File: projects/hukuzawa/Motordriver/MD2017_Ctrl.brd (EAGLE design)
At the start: 65 x 65 mm, 18 parts, among them IC1 PIC16F648, J1 3X2A, Q1 CERALOCK

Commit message: モータドライバ制御部 ボード図一時完成
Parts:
- moved U$2 42.9 mm to (45.5, 4.00), turned to 180 degrees
- moved D3 39.0 mm to (59.0, 19.0), turned to 270 degrees
- moved POWERPPORT 27.5 mm to (67.0, 18.0), turned to 90 degrees
- moved POWERNPORT 24.2 mm to (3.00, 18.0), turned to 90 degrees
- moved U$3 21.6 mm to (14.0, 13.0), turned to 270 degrees
- moved Q1 16.4 mm to (32.5, 54.5), turned to 0 degrees
- moved D4 12.2 mm to (30.0, 18.5), turned to 90 degrees
- moved C2 6.96 mm to (57.0, 45.5)
- moved C1 6.80 mm to (62.5, 45.5)
- moved C3 6.80 mm to (52.0, 45.5)
- moved J1 6.36 mm to (66.0, 58.0)
- moved NJM1 5.85 mm to (60.0, 51.0)
- moved IC1 5.52 mm to (35.0, 45.5)
- moved D2 5.32 mm to (49.5, 24.0)
- moved SIGNALPORT 5.15 mm to (35.0, 65.0)
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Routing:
- net GND: track 0.00 -> 159.0 mm, vias 0 -> 4
- net 5V: track 0.00 -> 94.9 mm
- net N$3: track 0.00 -> 67.1 mm
- net N$7: track 0.00 -> 49.6 mm
- net SIGNAL: track 0.00 -> 46.1 mm, vias 0 -> 2
- net N$6: track 0.00 -> 40.7 mm
- net N$5: track 0.00 -> 35.8 mm
- net N$2: track 0.00 -> 35.6 mm
- net N$4: track 0.00 -> 35.5 mm
- net BDIR: track 0.00 -> 32.3 mm, vias 0 -> 2
- net ADIR: track 0.00 -> 22.0 mm, vias 0 -> 2
- net BPWM: track 0.00 -> 19.5 mm
- net BD/B: track 0.00 -> 19.5 mm
- net APWM: track 0.00 -> 19.5 mm
- net 9VIN: track 0.00 -> 18.6 mm
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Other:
- board size 65 x 65 mm -> 70 x 70 mm

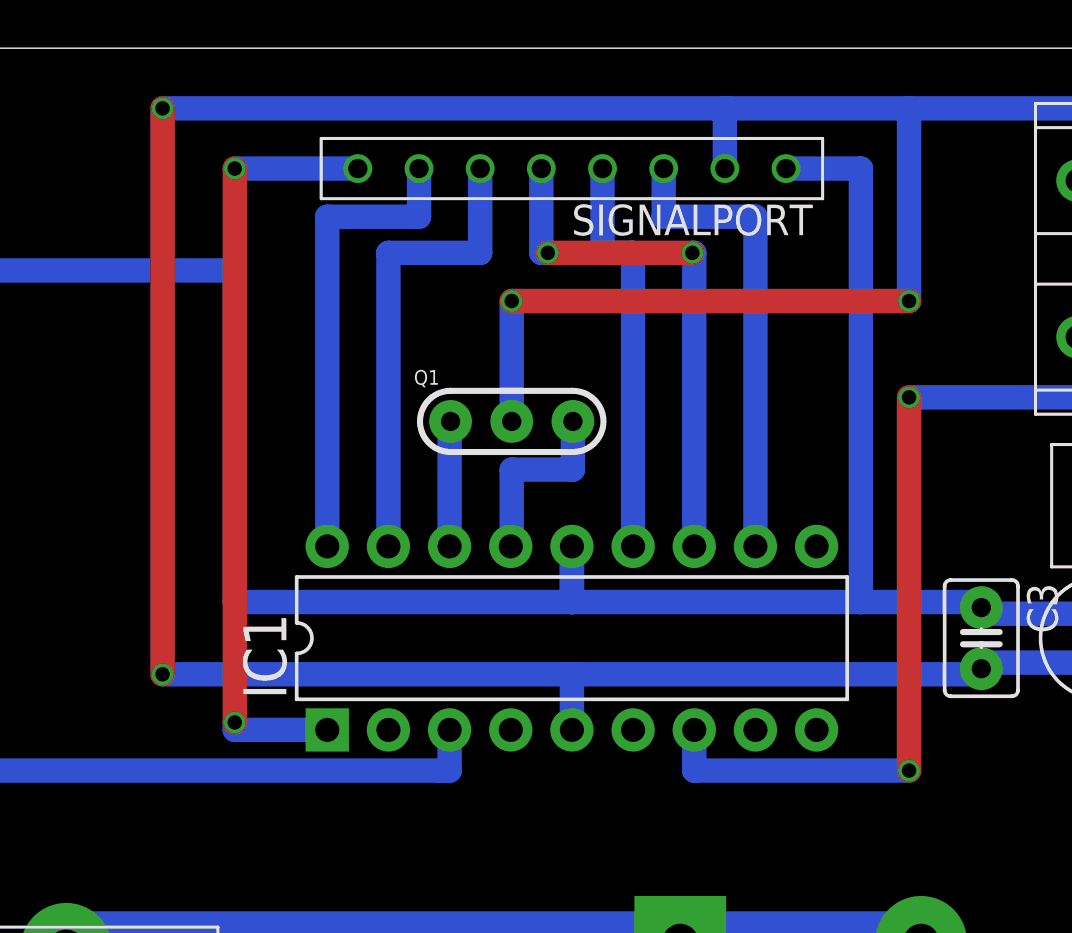
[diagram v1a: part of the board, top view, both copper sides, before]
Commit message: モータードライバ修正
モータードライバのジャンパ線部のドリル径を修正
それに伴って一部の配置の修正
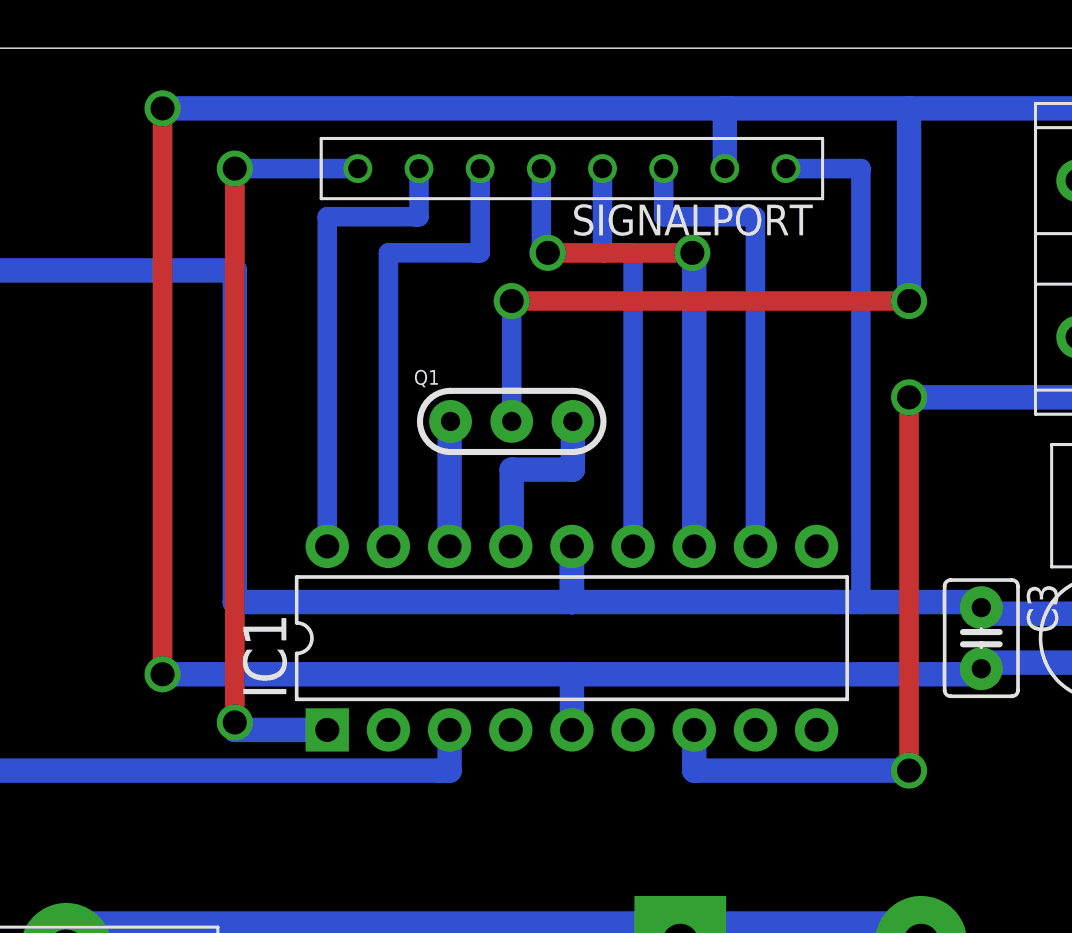
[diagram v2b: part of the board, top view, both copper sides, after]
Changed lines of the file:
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@@
 <wire x1="47" y1="47" x2="52" y2="47" width="1.016" layer="16"/>
 <wire x1="52" y1="47" x2="52" y2="46.77" width="1.016" layer="16"/>
-<wire x1="43.89" y1="65" x2="47" y2="65" width="1.016" layer="16"/>
-<wire x1="47" y1="65" x2="47" y2="47" width="1.016" layer="16"/>
+<wire x1="43.89" y1="65" x2="47" y2="65" width="0.8128" layer="16"/>
+<wire x1="47" y1="65" x2="47" y2="47" width="0.8128" layer="16"/>
 </signal>
 <signal name="9VIN">
@@
 <wire x1="40.08" y1="41.69" x2="40.08" y2="40" width="1.016" layer="16"/>
 <wire x1="40.08" y1="40" x2="49" y2="40" width="1.016" layer="16"/>
-<via x="49" y="40" extent="1-16" drill="0.6" shape="square"/>
-<wire x1="49" y1="40" x2="49" y2="55.5" width="1.016" layer="1"/>
-<via x="49" y="55.5" extent="1-16" drill="0.6" shape="square"/>
+<via x="49" y="40" extent="1-16" drill="1"/>
+<wire x1="49" y1="40" x2="49" y2="55.5" width="0.8128" layer="1"/>
+<via x="49" y="55.5" extent="1-16" drill="1"/>
 <wire x1="49" y1="55.5" x2="60" y2="55.5" width="1.016" layer="16"/>
 <wire x1="60" y1="55.5" x2="60" y2="58" width="1.016" layer="16"/>
@@
 <wire x1="35" y1="41.69" x2="35" y2="44" width="1.016" layer="16"/>
 <wire x1="35" y1="44" x2="18" y2="44" width="1.016" layer="16"/>
-<via x="18" y="44" extent="1-16" drill="0.6" shape="square"/>
-<wire x1="18" y1="44" x2="18" y2="67.5" width="1.016" layer="1"/>
-<via x="18" y="67.5" extent="1-16" drill="0.6" shape="square"/>
+<via x="18" y="44" extent="1-16" drill="1"/>
+<wire x1="18" y1="44" x2="18" y2="67.5" width="0.8128" layer="1"/>
+<via x="18" y="67.5" extent="1-16" drill="1"/>
 <wire x1="18" y1="67.5" x2="41.5" y2="67.5" width="1.016" layer="16"/>
 <wire x1="35" y1="44" x2="52" y2="44" width="1.016" layer="16"/>
 <wire x1="52" y1="44" x2="52" y2="44.23" width="1.016" layer="16"/>
-<wire x1="32.5" y1="54.5" x2="32.5" y2="59.5" width="1.016" layer="16"/>
-<via x="32.5" y="59.5" extent="1-16" drill="0.6" shape="square"/>
-<wire x1="32.5" y1="59.5" x2="49" y2="59.5" width="1.016" layer="1"/>
-<via x="49" y="59.5" extent="1-16" drill="0.6" shape="square"/>
+<wire x1="32.5" y1="54.5" x2="32.5" y2="59.5" width="0.8128" layer="16"/>
+<via x="32.5" y="59.5" extent="1-16" drill="1"/>
+<wire x1="32.5" y1="59.5" x2="49" y2="59.5" width="0.8128" layer="1"/>
+<via x="49" y="59.5" extent="1-16" drill="1"/>
 <wire x1="49" y1="59.5" x2="49" y2="67.5" width="1.016" layer="16"/>
 </signal>
@@
 <contactref element="SIGNALPORT" pad="3"/>
 <contactref element="IC1" pad="11"/>
-<wire x1="38.81" y1="65" x2="38.81" y2="63" width="1.016" layer="16"/>
-<wire x1="38.81" y1="63" x2="42.5" y2="63" width="1.016" layer="16"/>
-<wire x1="42.5" y1="63" x2="42.62" y2="63" width="1.016" layer="16"/>
-<wire x1="42.62" y1="63" x2="42.62" y2="49.31" width="1.016" layer="16"/>
+<wire x1="38.81" y1="65" x2="38.81" y2="63" width="0.8128" layer="16"/>
+<wire x1="38.81" y1="63" x2="42.5" y2="63" width="0.8128" layer="16"/>
+<wire x1="42.5" y1="63" x2="42.62" y2="63" width="0.8128" layer="16"/>
+<wire x1="42.62" y1="63" x2="42.62" y2="49.31" width="0.8128" layer="16"/>
 </signal>
 <signal name="AD/B">
 <contactref element="SIGNALPORT" pad="4"/>
 <contactref element="IC1" pad="13"/>
-<wire x1="36.27" y1="65" x2="36.27" y2="61.5" width="1.016" layer="16"/>
-<wire x1="36.27" y1="61.5" x2="37.5" y2="61.5" width="1.016" layer="16"/>
-<wire x1="37.5" y1="61.5" x2="37.54" y2="61.5" width="1.016" layer="16"/>
-<wire x1="37.54" y1="61.5" x2="37.54" y2="49.31" width="1.016" layer="16"/>
+<wire x1="36.27" y1="65" x2="36.27" y2="61.5" width="0.8128" layer="16"/>
+<wire x1="36.27" y1="61.5" x2="37.5" y2="61.5" width="0.8128" layer="16"/>
+<wire x1="37.5" y1="61.5" x2="37.54" y2="61.5" width="0.8128" layer="16"/>
+<wire x1="37.54" y1="61.5" x2="37.54" y2="49.31" width="0.8128" layer="16"/>
 </signal>
 <signal name="ADIR">
 <contactref element="SIGNALPORT" pad="5"/>
 <contactref element="IC1" pad="12"/>
-<wire x1="33.73" y1="65" x2="33.73" y2="61.5" width="1.016" layer="16"/>
+<wire x1="33.73" y1="65" x2="33.73" y2="61.5" width="0.8128" layer="16"/>
 <wire x1="33.73" y1="61.5" x2="34" y2="61.5" width="1.016" layer="16"/>
-<via x="34" y="61.5" extent="1-16" drill="0.6" shape="square"/>
-<wire x1="34" y1="61.5" x2="40" y2="61.5" width="1.016" layer="1"/>
-<via x="40" y="61.5" extent="1-16" drill="0.6" shape="square"/>
+<via x="34" y="61.5" extent="1-16" drill="1"/>
+<wire x1="34" y1="61.5" x2="40" y2="61.5" width="0.8128" layer="1"/>
+<via x="40" y="61.5" extent="1-16" drill="1"/>
 <wire x1="40" y1="61.5" x2="40.08" y2="61.5" width="1.016" layer="16"/>
 <wire x1="40.08" y1="61.5" x2="40.08" y2="49.31" width="1.016" layer="16"/>
@@
 <contactref element="SIGNALPORT" pad="6"/>
 <contactref element="IC1" pad="17"/>
-<wire x1="27.38" y1="49.31" x2="27.38" y2="61.5" width="1.016" layer="16"/>
-<wire x1="27.38" y1="61.5" x2="31" y2="61.5" width="1.016" layer="16"/>
-<wire x1="31" y1="61.5" x2="31.19" y2="61.5" width="1.016" layer="16"/>
-<wire x1="31.19" y1="61.5" x2="31.19" y2="65" width="1.016" layer="16"/>
+<wire x1="27.38" y1="49.31" x2="27.38" y2="61.5" width="0.8128" layer="16"/>
+<wire x1="27.38" y1="61.5" x2="31" y2="61.5" width="0.8128" layer="16"/>
+<wire x1="31" y1="61.5" x2="31.19" y2="61.5" width="0.8128" layer="16"/>
+<wire x1="31.19" y1="61.5" x2="31.19" y2="65" width="0.8128" layer="16"/>
 </signal>
 <signal name="BD/B">
 <contactref element="SIGNALPORT" pad="7"/>
 <contactref element="IC1" pad="18"/>
-<wire x1="24.84" y1="49.31" x2="24.84" y2="63" width="1.016" layer="16"/>
-<wire x1="24.84" y1="63" x2="28.5" y2="63" width="1.016" layer="16"/>
-<wire x1="28.5" y1="63" x2="28.65" y2="63" width="1.016" layer="16"/>
-<wire x1="28.65" y1="63" x2="28.65" y2="65" width="1.016" layer="16"/>
+<wire x1="24.84" y1="49.31" x2="24.84" y2="63" width="0.8128" layer="16"/>
+<wire x1="24.84" y1="63" x2="28.5" y2="63" width="0.8128" layer="16"/>
+<wire x1="28.5" y1="63" x2="28.65" y2="63" width="0.8128" layer="16"/>
+<wire x1="28.65" y1="63" x2="28.65" y2="65" width="0.8128" layer="16"/>
 </signal>
 <signal name="BDIR">
 <contactref element="SIGNALPORT" pad="8"/>
 <contactref element="IC1" pad="1"/>
-<wire x1="26.11" y1="65" x2="21" y2="65" width="1.016" layer="16"/>
-<via x="21" y="65" extent="1-16" drill="0.6" shape="square"/>
-<wire x1="21" y1="65" x2="21" y2="42" width="1.016" layer="1"/>
-<via x="21" y="42" extent="1-16" drill="0.6" shape="square"/>
+<wire x1="26.11" y1="65" x2="21" y2="65" width="0.8128" layer="16"/>
+<via x="21" y="65" extent="1-16" drill="1"/>
+<wire x1="21" y1="65" x2="21" y2="42" width="0.8128" layer="1"/>
+<via x="21" y="42" extent="1-16" drill="1"/>
 <wire x1="21" y1="42" x2="21" y2="41.69" width="1.016" layer="16"/>
 <wire x1="21" y1="41.69" x2="24.84" y2="41.69" width="1.016" layer="16"/>

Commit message: モータードライバ修正
穴径を1.0～1.2mmの範囲に収まるよう修正
Dimensionラインの太さを0に修正
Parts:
- D1, D2, D3, D4: device FP-21T for MITS:DO201-15 -> diode:DO201-15
- moved D1 14.4 mm to (25.5, 20.5)
- moved D4 13.5 mm to (41.5, 11.5), turned to 180 degrees
- moved D2 9.71 mm to (41.5, 29.5), turned to 180 degrees
- moved D3 1.80 mm to (58.0, 20.5)
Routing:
- net N$6: track 40.7 -> 15.3 mm
- net N$5: track 35.8 -> 22.2 mm
- net N$7: track 49.6 -> 37.0 mm
- net N$3: track 67.1 -> 55.7 mm
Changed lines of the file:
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@@
 <element name="POWERPPORT" library="FH105" package="FH105-1X8SG" value="8PIN" x="67" y="18" rot="R90"/>
 <element name="J1" library="3M_372xx" package="37206-62A3-003" value="3X2A" x="66" y="58" rot="R90"/>
-<element name="D1" library="FP-21T for MITS" package="DO201-15" value="Z-DIODE" x="39.5" y="24" rot="R270"/>
-<element name="D2" library="FP-21T for MITS" package="DO201-15" value="Z-DIODE" x="49.5" y="24" rot="R90"/>
-<element name="D3" library="FP-21T for MITS" package="DO201-15" value="Z-DIODE" x="59" y="19" rot="R270"/>
-<element name="D4" library="FP-21T for MITS" package="DO201-15" value="Z-DIODE" x="30" y="18.5" rot="R90"/>
 <element name="LED1" library="FP-21T for MITS" package="LED5MM" value="" x="7" y="59.5" rot="R270"/>
 <element name="R1" library="rcl" package="R3216W" value="" x="7" y="52.5" rot="MR90"/>
@@
 <element name="C2" library="FP-21T for MITS" package="E2-5" value="" x="57" y="45.5" rot="R270"/>
 <element name="C3" library="FP-21T for MITS" package="C0.1UF" value="C0.1UF" x="52" y="45.5" rot="R270"/>
+<element name="D1" library="diode" package="DO201-15" value="Z-DIODE" x="25.5" y="20.5" rot="R270"/>
+<element name="D2" library="diode" package="DO201-15" value="Z-DIODE" x="41.5" y="29.5" rot="R180"/>
+<element name="D3" library="diode" package="DO201-15" value="Z-DIODE" x="58" y="20.5" rot="R270"/>
+<element name="D4" library="diode" package="DO201-15" value="Z-DIODE" x="41.5" y="11.5" rot="R180"/>
 </elements>
 <signals>
@@
 </signal>
 <signal name="N$3">
-<contactref element="D1" pad="A"/>
-<contactref element="D4" pad="A"/>
 <contactref element="POWERNPORT" pad="1"/>
 <contactref element="POWERNPORT" pad="8"/>
@@
 <contactref element="POWERNPORT" pad="6"/>
 <contactref element="POWERNPORT" pad="7"/>
-<wire x1="30" y1="27.39" x2="39.5" y2="27.39" width="2.54" layer="16"/>
-<wire x1="39.5" y1="27.39" x2="39.5" y2="15.11" width="2.54" layer="16"/>
 <wire x1="3" y1="26.89" x2="3" y2="27.39" width="2.54" layer="16"/>
-<wire x1="3" y1="27.39" x2="30" y2="27.39" width="2.54" layer="16"/>
 <wire x1="3" y1="26.89" x2="3" y2="24.35" width="2.54" layer="16"/>
 <wire x1="3" y1="24.35" x2="3" y2="21.81" width="2.54" layer="16"/>
@@
 <wire x1="3" y1="14.19" x2="3" y2="11.65" width="2.54" layer="16"/>
 <wire x1="3" y1="11.65" x2="3" y2="9.11" width="2.54" layer="16"/>
+<contactref element="D1" pad="A"/>
+<contactref element="D4" pad="A"/>
+<wire x1="32.61" y1="11.5" x2="25.5" y2="11.5" width="2.1844" layer="16"/>
+<wire x1="25.5" y1="11.5" x2="25.5" y2="11.61" width="2.1844" layer="16"/>
+<wire x1="25.5" y1="11.61" x2="25.5" y2="19.27" width="2.1844" layer="16"/>
+<wire x1="25.5" y1="19.27" x2="3" y2="19.27" width="2.1844" layer="16"/>
 </signal>
 <signal name="N$5">
+<contactref element="U$3" pad="1"/>
+<wire x1="14" y1="32.89" x2="14" y2="32.6" width="2.54" layer="16"/>
 <contactref element="D1" pad="C"/>
 <contactref element="D2" pad="A"/>
-<contactref element="U$3" pad="1"/>
-<wire x1="49.5" y1="32.89" x2="39.5" y2="32.89" width="2.54" layer="16"/>
-<wire x1="39.5" y1="32.89" x2="14" y2="32.89" width="2.54" layer="16"/>
-<wire x1="14" y1="32.89" x2="14" y2="32.6" width="2.54" layer="16"/>
+<wire x1="25.5" y1="29.39" x2="25.5" y2="29.5" width="2.1844" layer="16"/>
+<wire x1="25.5" y1="29.5" x2="32.61" y2="29.5" width="2.1844" layer="16"/>
+<wire x1="25.5" y1="29.39" x2="25.5" y2="32.6" width="2.1844" layer="16"/>
+<wire x1="25.5" y1="32.6" x2="14" y2="32.6" width="2.1844" layer="16"/>
 </signal>
 <signal name="N$6">
+<contactref element="U$2" pad="P1"/>
+<contactref element="D3" pad="A"/>
 <contactref element="D4" pad="C"/>
-<contactref element="D3" pad="A"/>
-<contactref element="U$2" pad="P1"/>
-<wire x1="30" y1="9.61" x2="50.5" y2="9.61" width="2.54" layer="16"/>
-<wire x1="50.5" y1="9.61" x2="50.5" y2="4" width="2.54" layer="16"/>
-<wire x1="59" y1="10.11" x2="50.5" y2="10.11" width="2.54" layer="16"/>
-<wire x1="50.5" y1="10.11" x2="50.5" y2="4" width="2.54" layer="16"/>
+<wire x1="50.39" y1="11.5" x2="58" y2="11.5" width="2.1844" layer="16"/>
+<wire x1="58" y1="11.5" x2="58" y2="11.61" width="2.1844" layer="16"/>
+<wire x1="50.5" y1="4" x2="50.5" y2="11.5" width="2.1844" layer="16"/>
+<wire x1="50.5" y1="11.5" x2="50.39" y2="11.5" width="2.1844" layer="16"/>
 </signal>
 <signal name="N$7">
 <contactref element="POWERPPORT" pad="8"/>
 <contactref element="POWERPPORT" pad="1"/>
-<contactref element="D2" pad="C"/>
-<contactref element="D3" pad="C"/>
 <contactref element="POWERPPORT" pad="2"/>
 <contactref element="POWERPPORT" pad="3"/>
@@
 <wire x1="67" y1="21.81" x2="67" y2="24.35" width="2.54" layer="16"/>
 <wire x1="67" y1="24.35" x2="67" y2="26.89" width="2.54" layer="16"/>
-<wire x1="59" y1="27.89" x2="59.5" y2="27.89" width="2.54" layer="16"/>
-<wire x1="59.5" y1="27.89" x2="67" y2="27.89" width="2.54" layer="16"/>
-<wire x1="67" y1="27.89" x2="67" y2="26.89" width="2.54" layer="16"/>
-<wire x1="49.5" y1="15.11" x2="49.5" y2="27.89" width="2.54" layer="16"/>
-<wire x1="49.5" y1="27.89" x2="59.5" y2="27.89" width="2.54" layer="16"/>
+<contactref element="D2" pad="C"/>
+<contactref element="D3" pad="C"/>
+<wire x1="58" y1="29.39" x2="67" y2="29.39" width="2.1844" layer="16"/>
+<wire x1="67" y1="29.39" x2="67" y2="26.89" width="2.1844" layer="16"/>
+<wire x1="58" y1="29.39" x2="58" y2="29.5" width="2.1844" layer="16"/>
+<wire x1="58" y1="29.5" x2="50.39" y2="29.5" width="2.1844" layer="16"/>
 </signal>
 <signal name="N$4">
